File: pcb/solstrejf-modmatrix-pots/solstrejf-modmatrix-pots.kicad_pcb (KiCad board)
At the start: 2 copper layers, 165.1 x 229.9 mm, 56 parts, among them J1 Conn_02x08_Counter_Clockwise, J2 Conn_02x08_Counter_Clockwise, J3 Conn_02x08_Counter_Clockwise, J4 Conn_02x08_Counter_Clockwise

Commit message: Updated voice board front-panel and mod-matrix
Created new dimensions to get a better physical layout of the 4x voice board control panels and the mod-matrix.
Exported .wrl 3D models of voice board front-panel and mod-matrix to create a MeshLab view.
Added MeshLab project files and new images aswell.
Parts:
- added G***: LOGO, LOGO, F.Cu at (67.3, 18.8)
- H1, H2, H3, H4: footprint MountingHole:MountingHole_3.2mm_M3 -> MountingHole:MountingHole_3.2mm_M3_DIN965
- moved H3 18.6 mm to (-11.6, 254.8)
- moved H4 18.6 mm to (146.2, 254.8)
- moved J1 11.7 mm to (17.8, 247.3)
- moved J2 11.7 mm to (56.5, 247.4)
- moved J3 11.7 mm to (95.2, 247.4)
- moved J4 11.7 mm to (134.0, 247.3)
- moved RV10 11.7 mm to (-3.77, 195.5)
- moved RV11 11.7 mm to (7.02, 195.5)
- moved RV12 11.7 mm to (17.8, 195.5)
- moved RV16 11.7 mm to (35.0, 90.1)
- moved RV17 11.7 mm to (45.8, 90.1)
- moved RV18 11.7 mm to (56.6, 90.1)
- moved RV22 11.7 mm to (35.0, 195.5)
- moved RV23 11.7 mm to (45.8, 195.5)
- moved RV24 11.7 mm to (56.6, 195.5)
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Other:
- board size 165.1 x 229.9 mm -> 165.1 x 246.9 mm

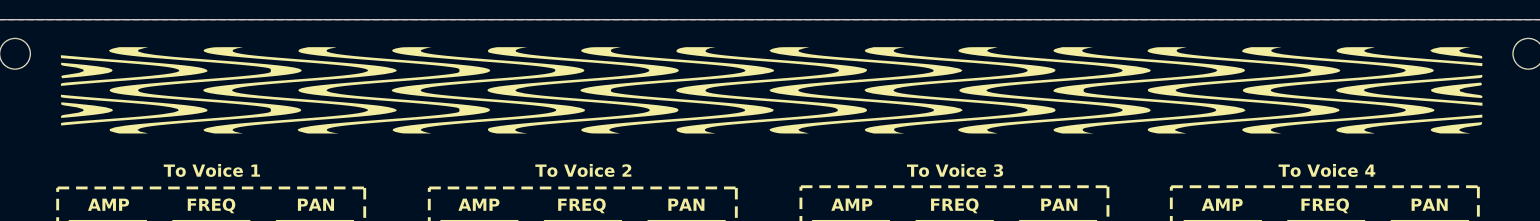
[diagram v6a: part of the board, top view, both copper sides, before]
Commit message: Updated mod-matrix PCB to have a hole for master volume pot
Added a M8 hole in the mod-matrix PCB to be able to attach the stereo master volume control.
Updated the images of the mod-matrix and the meshlab render.
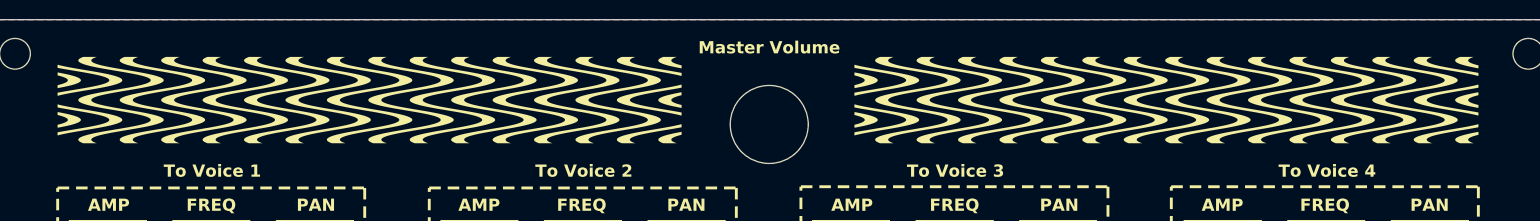
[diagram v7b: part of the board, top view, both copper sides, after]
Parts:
- removed the G*** at (67.3, 18.8)
- added G***: LOGO, LOGO, F.Cu at (25.4, 19.8)
- added G***: LOGO, LOGO, F.Cu at (108.5, 19.8)
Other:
- outline, holes or cut-outs redrawn
- board text added: "Master Volume"
- board text added: "Mounting hole for stereo 16mm master volume potentiometer // connects to PSU+Mixer board //"

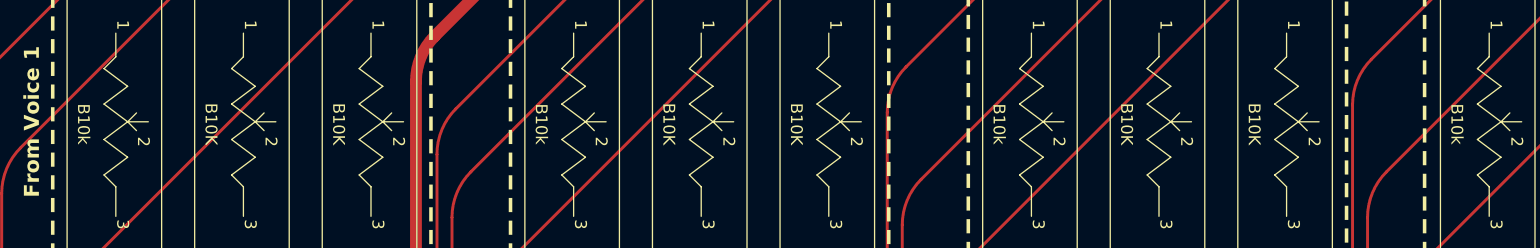
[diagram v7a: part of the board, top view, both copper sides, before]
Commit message: Updated potentiometer value from B10k to B10K in order for all of the slide pots to have the same value in the BOM. Generated ibom for the mod-matrix board.
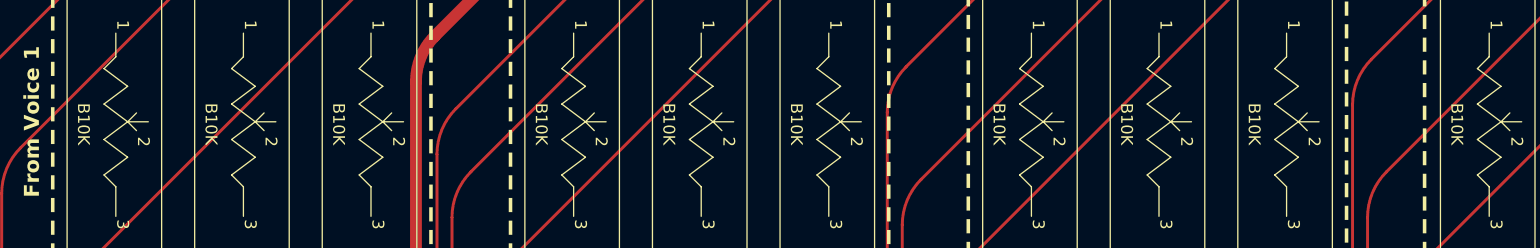
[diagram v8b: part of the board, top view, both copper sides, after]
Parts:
- RV1, RV13, RV25, RV37: value B10k -> B10K
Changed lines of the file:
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@@
 	)
 	(paper "A4")
+	(title_block
+		(title "Solstrejf Modulation Matrix")
+		(date "2024-11-02")
+		(rev "1.0")
+	)
 	(layers
 		(0 "F.Cu" signal)
@@
 			)
 		)
-		(property "Value" "B10k"
+		(property "Value" "B10K"
 			(at 17.1958 0.7366 -90)
 			(unlocked yes)
@@
 			)
 		)
-		(property "Value" "B10k"
+		(property "Value" "B10K"
 			(at 17.1958 0.7366 -90)
 			(unlocked yes)
@@
 			)
 		)
-		(property "Value" "B10k"
+		(property "Value" "B10K"
 			(at 17.1958 0.7366 -90)
 			(unlocked yes)
@@
 			)
 		)
-		(property "Value" "B10k"
+		(property "Value" "B10K"
 			(at 17.1958 0.7366 -90)
 			(unlocked yes)
